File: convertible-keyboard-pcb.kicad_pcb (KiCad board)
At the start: 2 copper layers, 383 parts, among them J1 USB_C, Q1 AO3400A, Q2 2N7002, Q3 2N7002, SW1 SW_MX_LED, SW10 SW_MX_LED, SW100 SW_MX_LED, SW101 SW_MX_LED, SW102 SW_MX_LED, SW103 SW_MX_LED, SW104 SW_MX_LED, SW105 SW_MX_LED, SW106 SW_Push, SW107 SW_MX_LED, SW108 SW_MX_LED, SW11 SW_MX_LED, SW12 SW_MX_LED, SW13 SW_MX_LED, SW14 SW_MX_LED, SW15 SW_MX_LED, SW16 SW_MX_LED, SW17 SW_MX_LED, SW18 SW_MX_LED, SW19 SW_MX_LED, SW2 SW_MX_LED, SW20 SW_MX_LED, SW201 SW_Push, SW202 SW_Push, SW21 SW_MX_LED, SW22 SW_MX_LED, SW23 SW_MX_LED, SW24 SW_MX_LED, SW25 SW_MX_LED, SW26 SW_MX_LED, SW27 SW_MX_LED, SW28 SW_MX_LED, SW29 SW_MX_LED, SW3 SW_MX_LED, SW30 SW_MX_LED, SW31 SW_MX_LED, SW32 SW_MX_LED, SW33 SW_MX_LED, SW34 SW_MX_LED, SW35 SW_MX_LED, SW36 SW_MX_LED, SW37 SW_MX_LED, SW38 SW_MX_LED, SW39 SW_MX_LED, SW4 SW_MX_LED, SW40 SW_MX_LED, SW41 SW_MX_LED, SW42 SW_MX_LED, SW43 SW_MX_LED, SW44 SW_MX_LED, SW45 SW_MX_LED, SW46 SW_MX_LED, SW47 SW_MX_LED, SW48 SW_MX_LED, SW49 SW_MX_LED, SW5 SW_MX_LED, SW50 SW_MX_LED, SW51 SW_MX_LED, SW52 SW_MX_LED, SW53 SW_MX_LED, SW54 SW_MX_LED, SW55 SW_MX_LED, SW56 SW_MX_LED, SW57 SW_MX_LED, SW58 SW_MX_LED, SW59 SW_MX_LED, SW6 SW_MX_LED, SW60 SW_MX_LED, SW61 SW_MX_LED, SW62 SW_MX_LED, SW63 SW_MX_LED, SW64 SW_MX_LED, SW65 SW_MX_LED, SW66 SW_MX_LED, SW67 SW_MX_LED, SW68 SW_MX_LED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

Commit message: Lock-Anzeigen nur noch als 0805, TKL nur Caps Lock über BildAuf
- 3-mm-THT-Varianten entfernt (D121, D123, D125, D127)
- Über dem Numpad: D128 Num und D126 Caps mittig auf Höhe der F-Reihe,
  bestückt
- TKL: nur noch Caps Lock (D122, DNP) mittig über BildAuf in der Lücke
  zwischen F-Reihe und Zahlenreihe – Num Lock fällt mit dem Numpad ohnehin
  weg, daher Num-Anzeige D124 samt R128 entfernt
- Direkt in KiCad-Dateien geändert, nicht über tools/ – Generator-Stand
  endet mit 2eb5d4f (in tools/README und CLAUDE.md vermerkt)

ERC 0, Parität sauber, DRC ohne neue Meldungen.

Co-Authored-By: Claude Opus 5 (1M context) <noreply@anthropic.com>
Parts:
- removed D121, D123, D125, D127: 3mm, LED_THT:LED_D3.0mm
- removed D124: 0805, LED_SMD:LED_0805_2012Metric
- removed R128: 1k, Resistor_SMD:R_0603_1608Metric
- moved D122 10.4 mm to (366.7, 52.4)
- moved R127 8.82 mm to (370.7, 52.4)
- moved D126 3.40 mm to (428.6, 38.1)
- moved D128 3.40 mm to (409.6, 38.1)
- moved R130 2.26 mm to (413.6, 38.1)
- moved R129 2.24 mm to (432.6, 38.1)

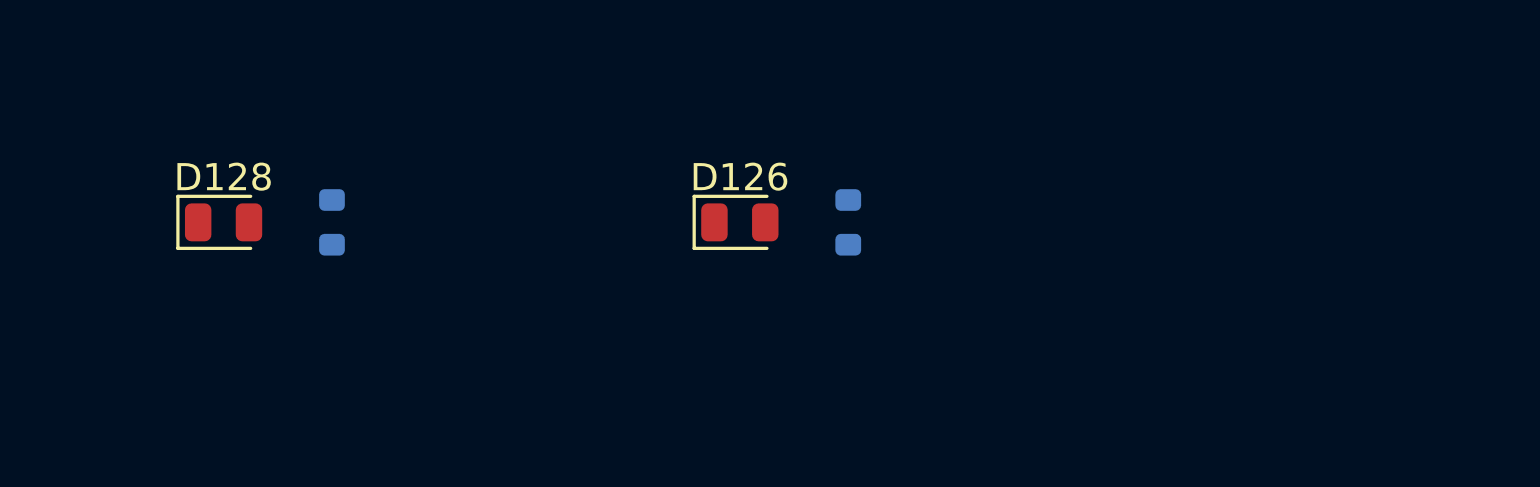
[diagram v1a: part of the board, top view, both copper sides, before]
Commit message: Lock-Anzeigen über dem Numpad rechtsbündig
Num Lock (D128) über *, Caps Lock (D126) über -, wie bei den meisten
Tastaturen; Vorwiderstände auf der Rückseite mitverschoben.

Co-Authored-By: Claude Opus 5 (1M context) <noreply@anthropic.com>
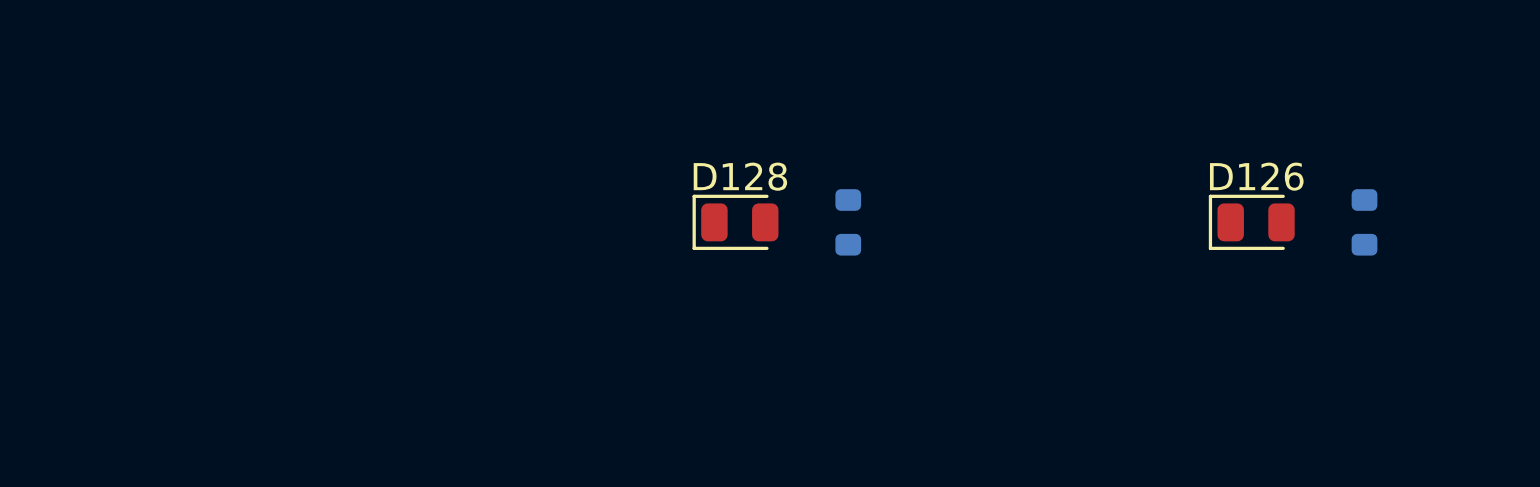
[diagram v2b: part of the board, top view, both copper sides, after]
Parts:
- moved D126 19.1 mm to (447.7, 38.1)
- moved D128 19.1 mm to (428.6, 38.1)
- moved R129 19.1 mm to (451.7, 38.1)
- moved R130 19.1 mm to (432.6, 38.1)
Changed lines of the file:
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@@
 	(footprint "LED_SMD:LED_0805_2012Metric"
 		(layer "F.Cu")
-		(at 409.575 38.1)
+		(at 428.625 38.1)
 		(descr "LED SMD 0805 (2012 Metric), square (rectangular) end terminal, IPC-7351 nominal, (Body size source: https://docs.google.com/spreadsheets/d/1BsfQQcO9C6DZCsRaXUlFlo91Tg2WpOkGARC1WS5S8t0/edit?usp=sharing)")
 		(tags "LED")
@@
 	(footprint "LED_SMD:LED_0805_2012Metric"
 		(layer "F.Cu")
-		(at 428.625 38.1)
+		(at 447.675 38.1)
 		(descr "LED SMD 0805 (2012 Metric), square (rectangular) end terminal, IPC-7351 nominal, (Body size source: https://docs.google.com/spreadsheets/d/1BsfQQcO9C6DZCsRaXUlFlo91Tg2WpOkGARC1WS5S8t0/edit?usp=sharing)")
 		(tags "LED")
@@
 	(footprint "Resistor_SMD:R_0603_1608Metric"
 		(layer "B.Cu")
-		(at 432.625 38.1 90)
+		(at 451.675 38.1 90)
 		(descr "Resistor SMD 0603 (1608 Metric), square (rectangular) end terminal, IPC-7351 nominal, (Body size source: IPC-SM-782 page 72, https://www.pcb-3d.com/wordpress/wp-content/uploads/ipc-sm-782a_amendment_1_and_2.pdf)")
 		(tags "resistor")
@@
 	(footprint "Resistor_SMD:R_0603_1608Metric"
 		(layer "B.Cu")
-		(at 413.575 38.1 90)
+		(at 432.625 38.1 90)
 		(descr "Resistor SMD 0603 (1608 Metric), square (rectangular) end terminal, IPC-7351 nominal, (Body size source: IPC-SM-782 page 72, https://www.pcb-3d.com/wordpress/wp-content/uploads/ipc-sm-782a_amendment_1_and_2.pdf)")
 		(tags "resistor")

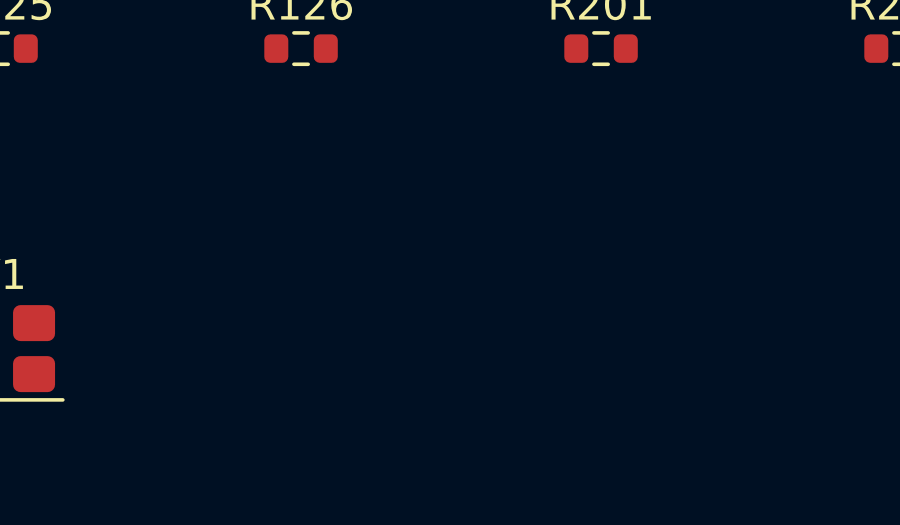
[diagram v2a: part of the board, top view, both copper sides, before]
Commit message: Anschlüsse für Unified Daughterboard (Pico-EZmate und JST-SH)
- J2 Molex Pico-EZmate 78171-0004 (uDB S1, C4, C5-EZM) und
  J3 JST-SH SM04B-SRSS-TB (uDB C3, C5-JSH), beide nicht bestückt
- Parallel zur USB-C-Buchse J1: Pin 1 VBUS, 2 D-, 3 D+, 4 + MP GND –
  Belegung aus den KiCad-Quellen von UDB-S und UDB-C-JSH gelesen (1:1-Kabel)
- J1 bleibt standardmäßig bestückt; für ein Daughterboard J1 weglassen und
  J2 oder J3 bestücken
- Footprints vorerst unplatziert neben den übrigen MCU-Bauteilen
- README (EN/DE) und CLAUDE.md ergänzt, LED-Entscheidung (THT oder
  Reverse-Mount-SMD) als offener Punkt vermerkt

ERC 0, Parität sauber, DRC ohne neue Meldungen.

Co-Authored-By: Claude Opus 5 (1M context) <noreply@anthropic.com>
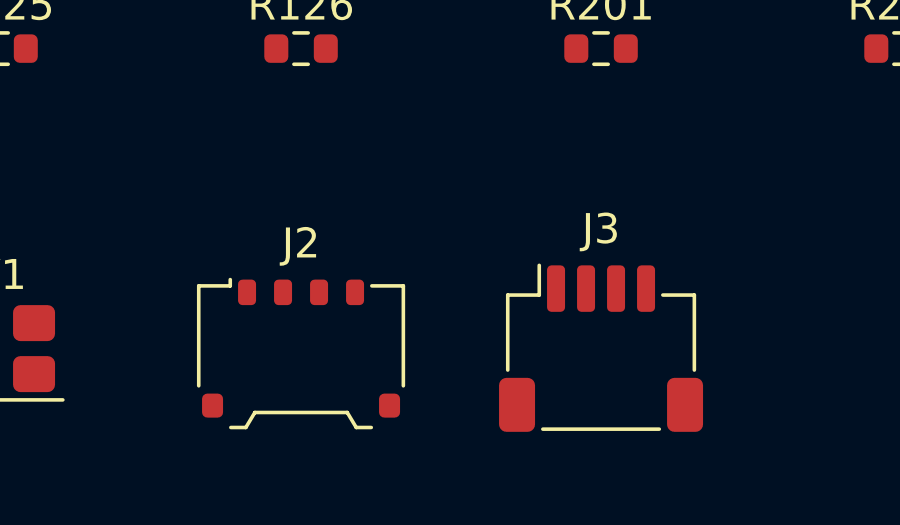
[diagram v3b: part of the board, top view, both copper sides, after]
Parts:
- added J2: Pico-EZmate 78171-0004, Connector_Molex:Molex_Pico-EZmate_78171-0004_1x04-1MP_P1.20mm_Vertical, F.Cu at (110.0, 195.0)
- added J3: JST-SH SM04B-SRSS-TB, Connector_JST:JST_SH_SM04B-SRSS-TB_1x04-1MP_P1.00mm_Horizontal, F.Cu at (120.0, 195.0)

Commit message: Tasten-LEDs als Reverse-Mount-SMD (Standard), THT-Variante vorgehalten
- Schalter wieder mit 2-Pin-Symbol und ai03-NoLED-Footprints; jede Taste
  hat eine eigene LED LEDn (gleiche Nummer) auf der Rückseite unter dem
  LED-Fenster (Schaltermitte +5,08 mm) – Drähte und Netze unverändert
- LED: XINGLIGHT XL-3216UWC-FB, weiß, LCSC C3646935, maschinell bestückt
- Eigener Footprint LED_1206_ReverseMount_XL-3216 nach dem JLC/EasyEDA-
  Footprint (Pads 1,0 x 1,524 mm bei +-1,651, Aussparung 2,2 x 1,9 mm):
  Pad-Innenkante 0,2 mm von der Aussparung, Eckradius 0,5 mm zum Fräsen.
  KiCads generischer Reverse-Mount-Footprint passt nicht zu diesem Teil
  (Loch in Längsrichtung kleiner als die Linse)
- convertible-keyboard-pcb.kicad_dru: 0,2 mm Kantenabstand nur an den
  LED-Aussparungen, sonst weiter 0,5 mm
- tools/led_variant.py smd|tht: tauscht nur die LED-Footprints; THT-Pads
  als MX_LED_THT/_FLIPPED in lib/keyboard.pretty, Hin- und Rückweg getestet
- Entfernt: Symbol SW_MX_LED, sym-lib-table, MXOnly-ISO-FLIPPED
  (FLIPPED-Sonderfälle entfallen mit den NoLED-Schaltern)
- README (EN/DE), tools/README, CLAUDE.md aktualisiert

ERC 0, Parität sauber, DRC ohne Fehler (nur bekannte Warnungen).

Co-Authored-By: Claude Opus 5 (1M context) <noreply@anthropic.com>
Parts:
- added LED1: XL-3216UWC-FB, keyboard:LED_1206_ReverseMount_XL-3216, B.Cu at (38.1, 43.2)
- added LED10: XL-3216UWC-FB, keyboard:LED_1206_ReverseMount_XL-3216, B.Cu at (247.7, 43.2)
- added LED100: XL-3216UWC-FB, keyboard:LED_1206_ReverseMount_XL-3216, B.Cu at (302.4, 148.0)
- added LED101: XL-3216UWC-FB, keyboard:LED_1206_ReverseMount_XL-3216, B.Cu at (328.6, 148.0)
- added LED102: XL-3216UWC-FB, keyboard:LED_1206_ReverseMount_XL-3216, B.Cu at (347.7, 148.0)
- added LED103: XL-3216UWC-FB, keyboard:LED_1206_ReverseMount_XL-3216, B.Cu at (366.7, 148.0)
- added LED104: XL-3216UWC-FB, keyboard:LED_1206_ReverseMount_XL-3216, B.Cu at (400.1, 148.0)
- added LED105: XL-3216UWC-FB, keyboard:LED_1206_ReverseMount_XL-3216, B.Cu at (428.6, 148.0)
- added LED107: XL-3216UWC-FB, keyboard:LED_1206_ReverseMount_XL-3216, B.Cu at (292.9, 109.9)
- added LED108: XL-3216UWC-FB, keyboard:LED_1206_ReverseMount_XL-3216, B.Cu at (50.0, 128.9)
- added LED11: XL-3216UWC-FB, keyboard:LED_1206_ReverseMount_XL-3216, B.Cu at (266.7, 43.2)
- added LED12: XL-3216UWC-FB, keyboard:LED_1206_ReverseMount_XL-3216, B.Cu at (285.8, 43.2)
- added LED13: XL-3216UWC-FB, keyboard:LED_1206_ReverseMount_XL-3216, B.Cu at (304.8, 43.2)
- added LED14: XL-3216UWC-FB, keyboard:LED_1206_ReverseMount_XL-3216, B.Cu at (328.6, 43.2)
- added LED15: XL-3216UWC-FB, keyboard:LED_1206_ReverseMount_XL-3216, B.Cu at (347.7, 43.2)
- added LED16: XL-3216UWC-FB, keyboard:LED_1206_ReverseMount_XL-3216, B.Cu at (366.7, 43.2)
- added LED17: XL-3216UWC-FB, keyboard:LED_1206_ReverseMount_XL-3216, B.Cu at (38.1, 71.8)
- added LED18: XL-3216UWC-FB, keyboard:LED_1206_ReverseMount_XL-3216, B.Cu at (57.1, 71.8)
- added LED19: XL-3216UWC-FB, keyboard:LED_1206_ReverseMount_XL-3216, B.Cu at (76.2, 71.8)
- added LED2: XL-3216UWC-FB, keyboard:LED_1206_ReverseMount_XL-3216, B.Cu at (76.2, 43.2)
- added LED20: XL-3216UWC-FB, keyboard:LED_1206_ReverseMount_XL-3216, B.Cu at (95.2, 71.8)
- added LED21: XL-3216UWC-FB, keyboard:LED_1206_ReverseMount_XL-3216, B.Cu at (114.3, 71.8)
- added LED22: XL-3216UWC-FB, keyboard:LED_1206_ReverseMount_XL-3216, B.Cu at (133.3, 71.8)
- added LED23: XL-3216UWC-FB, keyboard:LED_1206_ReverseMount_XL-3216, B.Cu at (152.4, 71.8)
- added LED24: XL-3216UWC-FB, keyboard:LED_1206_ReverseMount_XL-3216, B.Cu at (171.4, 71.8)
- added LED25: XL-3216UWC-FB, keyboard:LED_1206_ReverseMount_XL-3216, B.Cu at (190.5, 71.8)
- added LED26: XL-3216UWC-FB, keyboard:LED_1206_ReverseMount_XL-3216, B.Cu at (209.6, 71.8)
- added LED27: XL-3216UWC-FB, keyboard:LED_1206_ReverseMount_XL-3216, B.Cu at (228.6, 71.8)
- added LED28: XL-3216UWC-FB, keyboard:LED_1206_ReverseMount_XL-3216, B.Cu at (247.7, 71.8)
- added LED29: XL-3216UWC-FB, keyboard:LED_1206_ReverseMount_XL-3216, B.Cu at (266.7, 71.8)
- added LED3: XL-3216UWC-FB, keyboard:LED_1206_ReverseMount_XL-3216, B.Cu at (95.2, 43.2)
- added LED30: XL-3216UWC-FB, keyboard:LED_1206_ReverseMount_XL-3216, B.Cu at (295.3, 71.8)
- added LED31: XL-3216UWC-FB, keyboard:LED_1206_ReverseMount_XL-3216, B.Cu at (328.6, 71.8)
- added LED32: XL-3216UWC-FB, keyboard:LED_1206_ReverseMount_XL-3216, B.Cu at (347.7, 71.8)
- added LED33: XL-3216UWC-FB, keyboard:LED_1206_ReverseMount_XL-3216, B.Cu at (366.7, 71.8)
- added LED34: XL-3216UWC-FB, keyboard:LED_1206_ReverseMount_XL-3216, B.Cu at (390.5, 71.8)
- added LED35: XL-3216UWC-FB, keyboard:LED_1206_ReverseMount_XL-3216, B.Cu at (409.6, 71.8)
- added LED36: XL-3216UWC-FB, keyboard:LED_1206_ReverseMount_XL-3216, B.Cu at (428.6, 71.8)
- added LED37: XL-3216UWC-FB, keyboard:LED_1206_ReverseMount_XL-3216, B.Cu at (447.7, 71.8)
- added LED38: XL-3216UWC-FB, keyboard:LED_1206_ReverseMount_XL-3216, B.Cu at (42.9, 90.8)
- added LED39: XL-3216UWC-FB, keyboard:LED_1206_ReverseMount_XL-3216, B.Cu at (66.7, 90.8)
- added LED4: XL-3216UWC-FB, keyboard:LED_1206_ReverseMount_XL-3216, B.Cu at (114.3, 43.2)
- added LED40: XL-3216UWC-FB, keyboard:LED_1206_ReverseMount_XL-3216, B.Cu at (85.7, 90.8)
- added LED41: XL-3216UWC-FB, keyboard:LED_1206_ReverseMount_XL-3216, B.Cu at (104.8, 90.8)
- added LED42: XL-3216UWC-FB, keyboard:LED_1206_ReverseMount_XL-3216, B.Cu at (123.8, 90.8)
- added LED43: XL-3216UWC-FB, keyboard:LED_1206_ReverseMount_XL-3216, B.Cu at (142.9, 90.8)
- added LED44: XL-3216UWC-FB, keyboard:LED_1206_ReverseMount_XL-3216, B.Cu at (161.9, 90.8)
- added LED45: XL-3216UWC-FB, keyboard:LED_1206_ReverseMount_XL-3216, B.Cu at (181.0, 90.8)
- added LED46: XL-3216UWC-FB, keyboard:LED_1206_ReverseMount_XL-3216, B.Cu at (200.0, 90.8)
- added LED47: XL-3216UWC-FB, keyboard:LED_1206_ReverseMount_XL-3216, B.Cu at (219.1, 90.8)
- added LED48: XL-3216UWC-FB, keyboard:LED_1206_ReverseMount_XL-3216, B.Cu at (238.1, 90.8)
- added LED49: XL-3216UWC-FB, keyboard:LED_1206_ReverseMount_XL-3216, B.Cu at (257.2, 90.8)
- added LED5: XL-3216UWC-FB, keyboard:LED_1206_ReverseMount_XL-3216, B.Cu at (133.3, 43.2)
- added LED50: XL-3216UWC-FB, keyboard:LED_1206_ReverseMount_XL-3216, B.Cu at (276.2, 90.8)
- added LED51: XL-3216UWC-FB, keyboard:LED_1206_ReverseMount_XL-3216, B.Cu at (328.6, 90.8)
- added LED52: XL-3216UWC-FB, keyboard:LED_1206_ReverseMount_XL-3216, B.Cu at (347.7, 90.8)
- added LED53: XL-3216UWC-FB, keyboard:LED_1206_ReverseMount_XL-3216, B.Cu at (366.7, 90.8)
- added LED54: XL-3216UWC-FB, keyboard:LED_1206_ReverseMount_XL-3216, B.Cu at (390.5, 90.8)
- added LED55: XL-3216UWC-FB, keyboard:LED_1206_ReverseMount_XL-3216, B.Cu at (409.6, 90.8)
- added LED56: XL-3216UWC-FB, keyboard:LED_1206_ReverseMount_XL-3216, B.Cu at (428.6, 90.8)
- added LED57: XL-3216UWC-FB, keyboard:LED_1206_ReverseMount_XL-3216, B.Cu at (447.7, 100.3)
- added LED58: XL-3216UWC-FB, keyboard:LED_1206_ReverseMount_XL-3216, B.Cu at (45.2, 109.9)
- added LED59: XL-3216UWC-FB, keyboard:LED_1206_ReverseMount_XL-3216, B.Cu at (71.4, 109.9)
- added LED6: XL-3216UWC-FB, keyboard:LED_1206_ReverseMount_XL-3216, B.Cu at (161.9, 43.2)
- added LED60: XL-3216UWC-FB, keyboard:LED_1206_ReverseMount_XL-3216, B.Cu at (90.5, 109.9)
- added LED61: XL-3216UWC-FB, keyboard:LED_1206_ReverseMount_XL-3216, B.Cu at (109.5, 109.9)
- added LED62: XL-3216UWC-FB, keyboard:LED_1206_ReverseMount_XL-3216, B.Cu at (128.6, 109.9)
- added LED63: XL-3216UWC-FB, keyboard:LED_1206_ReverseMount_XL-3216, B.Cu at (147.6, 109.9)
- added LED64: XL-3216UWC-FB, keyboard:LED_1206_ReverseMount_XL-3216, B.Cu at (166.7, 109.9)
- added LED65: XL-3216UWC-FB, keyboard:LED_1206_ReverseMount_XL-3216, B.Cu at (185.7, 109.9)
- added LED66: XL-3216UWC-FB, keyboard:LED_1206_ReverseMount_XL-3216, B.Cu at (204.8, 109.9)
- added LED67: XL-3216UWC-FB, keyboard:LED_1206_ReverseMount_XL-3216, B.Cu at (223.8, 109.9)
- added LED68: XL-3216UWC-FB, keyboard:LED_1206_ReverseMount_XL-3216, B.Cu at (242.9, 109.9)
- added LED69: XL-3216UWC-FB, keyboard:LED_1206_ReverseMount_XL-3216, B.Cu at (261.9, 109.9)
- added LED7: XL-3216UWC-FB, keyboard:LED_1206_ReverseMount_XL-3216, B.Cu at (181.0, 43.2)
- added LED70: XL-3216UWC-FB, keyboard:LED_1206_ReverseMount_XL-3216, B.Cu at (281.0, 109.9)
- added LED71: XL-3216UWC-FB, keyboard:LED_1206_ReverseMount_XL-3216, B.Cu at (302.4, 100.3)
- added LED72: XL-3216UWC-FB, keyboard:LED_1206_ReverseMount_XL-3216, B.Cu at (390.5, 109.9)
- added LED73: XL-3216UWC-FB, keyboard:LED_1206_ReverseMount_XL-3216, B.Cu at (409.6, 109.9)
- added LED74: XL-3216UWC-FB, keyboard:LED_1206_ReverseMount_XL-3216, B.Cu at (428.6, 109.9)
- added LED75: XL-3216UWC-FB, keyboard:LED_1206_ReverseMount_XL-3216, B.Cu at (40.5, 128.9)
- added LED76: XL-3216UWC-FB, keyboard:LED_1206_ReverseMount_XL-3216, B.Cu at (61.9, 128.9)
- added LED77: XL-3216UWC-FB, keyboard:LED_1206_ReverseMount_XL-3216, B.Cu at (81.0, 128.9)
- added LED78: XL-3216UWC-FB, keyboard:LED_1206_ReverseMount_XL-3216, B.Cu at (100.0, 128.9)
- added LED79: XL-3216UWC-FB, keyboard:LED_1206_ReverseMount_XL-3216, B.Cu at (119.1, 128.9)
- added LED8: XL-3216UWC-FB, keyboard:LED_1206_ReverseMount_XL-3216, B.Cu at (200.0, 43.2)
- added LED80: XL-3216UWC-FB, keyboard:LED_1206_ReverseMount_XL-3216, B.Cu at (138.1, 128.9)
- added LED81: XL-3216UWC-FB, keyboard:LED_1206_ReverseMount_XL-3216, B.Cu at (157.2, 128.9)
- added LED82: XL-3216UWC-FB, keyboard:LED_1206_ReverseMount_XL-3216, B.Cu at (176.2, 128.9)
- added LED83: XL-3216UWC-FB, keyboard:LED_1206_ReverseMount_XL-3216, B.Cu at (195.3, 128.9)
- added LED84: XL-3216UWC-FB, keyboard:LED_1206_ReverseMount_XL-3216, B.Cu at (214.3, 128.9)
- added LED85: XL-3216UWC-FB, keyboard:LED_1206_ReverseMount_XL-3216, B.Cu at (233.4, 128.9)
- added LED86: XL-3216UWC-FB, keyboard:LED_1206_ReverseMount_XL-3216, B.Cu at (252.4, 128.9)
- added LED87: XL-3216UWC-FB, keyboard:LED_1206_ReverseMount_XL-3216, B.Cu at (288.1, 128.9)
- added LED88: XL-3216UWC-FB, keyboard:LED_1206_ReverseMount_XL-3216, B.Cu at (347.7, 128.9)
- added LED89: XL-3216UWC-FB, keyboard:LED_1206_ReverseMount_XL-3216, B.Cu at (390.5, 128.9)
- added LED9: XL-3216UWC-FB, keyboard:LED_1206_ReverseMount_XL-3216, B.Cu at (219.1, 43.2)
- added LED90: XL-3216UWC-FB, keyboard:LED_1206_ReverseMount_XL-3216, B.Cu at (409.6, 128.9)
- added LED91: XL-3216UWC-FB, keyboard:LED_1206_ReverseMount_XL-3216, B.Cu at (428.6, 128.9)
- added LED92: XL-3216UWC-FB, keyboard:LED_1206_ReverseMount_XL-3216, B.Cu at (447.7, 138.4)
- added LED93: XL-3216UWC-FB, keyboard:LED_1206_ReverseMount_XL-3216, B.Cu at (40.5, 148.0)
- added LED94: XL-3216UWC-FB, keyboard:LED_1206_ReverseMount_XL-3216, B.Cu at (64.3, 148.0)
- added LED95: XL-3216UWC-FB, keyboard:LED_1206_ReverseMount_XL-3216, B.Cu at (88.1, 148.0)
- added LED96: XL-3216UWC-FB, keyboard:LED_1206_ReverseMount_XL-3216, B.Cu at (159.5, 148.0)
- added LED97: XL-3216UWC-FB, keyboard:LED_1206_ReverseMount_XL-3216, B.Cu at (231.0, 148.0)
- added LED98: XL-3216UWC-FB, keyboard:LED_1206_ReverseMount_XL-3216, B.Cu at (254.8, 148.0)
- added LED99: XL-3216UWC-FB, keyboard:LED_1206_ReverseMount_XL-3216, B.Cu at (278.6, 148.0)
- SW1, SW10, SW101, SW102, SW103, SW105, SW11, SW12, SW13, SW14, SW15, SW16, SW17, SW18, SW19, SW2, SW20, SW21, SW22, SW23, SW24, SW25, SW26, SW27, SW28, SW29, SW3, SW31, SW32, SW33, SW34, SW35, SW36, SW37, SW39, SW4, SW40, SW41, SW42, SW43, SW44, SW45, SW46, SW47, SW48, SW49, SW5, SW50, SW51, SW52, SW53, SW54, SW55, SW56, SW59, SW6, SW60, SW61, SW62, SW63, SW64, SW65, SW66, SW67, SW68, SW69, SW7, SW70, SW72, SW73, SW74, SW77, SW78, SW79, SW8, SW80, SW81, SW82, SW83, SW84, SW85, SW86, SW88, SW89, SW9, SW90, SW91: value SW_MX_LED -> SW_Push; footprint MX_Only:MXOnly-1U -> MX_Only:MXOnly-1U-NoLED
- SW100, SW75, SW93, SW94, SW95, SW97, SW98, SW99: value SW_MX_LED -> SW_Push; footprint MX_Only:MXOnly-1.25U -> MX_Only:MXOnly-1.25U-NoLED
- SW104, SW30: value SW_MX_LED -> SW_Push; footprint MX_Only:MXOnly-2U -> MX_Only:MXOnly-2U-NoLED
- SW107: value SW_MX_LED -> SW_Push; footprint MX_Only:MXOnly-2.25U-FLIPPED -> MX_Only:MXOnly-2.25U-NoLED
- SW108: value SW_MX_LED -> SW_Push; footprint MX_Only:MXOnly-2.25U -> MX_Only:MXOnly-2.25U-NoLED
- SW38: value SW_MX_LED -> SW_Push; footprint MX_Only:MXOnly-1.5U -> MX_Only:MXOnly-1.5U-NoLED
- SW57, SW92: value SW_MX_LED -> SW_Push; footprint MX_Only:MXOnly-2U-VerticalStabilizers -> MX_Only:MXOnly-2U-VerticalStabilizers-NoLED
- SW58: value SW_MX_LED -> SW_Push; footprint MX_Only:MXOnly-1.75U -> MX_Only:MXOnly-1.75U-NoLED
- SW71: value SW_MX_LED -> SW_Push; footprint keyboard:MXOnly-ISO-FLIPPED -> MX_Only:MXOnly-ISO-NoLED
- SW76: value SW_MX_LED -> SW_Push; footprint MX_Only:MXOnly-1U-FLIPPED -> MX_Only:MXOnly-1U-NoLED
- SW87: value SW_MX_LED -> SW_Push; footprint MX_Only:MXOnly-2.75U -> MX_Only:MXOnly-2.75U-NoLED
- SW96: value SW_MX_LED -> SW_Push; footprint MX_Only:MXOnly-6.25U -> MX_Only:MXOnly-6.25U-NoLED
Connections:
- R1 pad 2: Net-(SW1B-A) -> Net-(LED1-A)
- R10 pad 2: Net-(SW10B-A) -> Net-(LED10-A)
- R100 pad 2: Net-(SW100B-A) -> Net-(LED100-A)
- R101 pad 2: Net-(SW101B-A) -> Net-(LED101-A)
- R102 pad 2: Net-(SW102B-A) -> Net-(LED102-A)
- R103 pad 2: Net-(SW103B-A) -> Net-(LED103-A)
- R104 pad 2: Net-(SW104B-A) -> Net-(LED104-A)
- R105 pad 2: Net-(SW105B-A) -> Net-(LED105-A)
- R107 pad 2: Net-(SW107B-A) -> Net-(LED107-A)
- R108 pad 2: Net-(SW108B-A) -> Net-(LED108-A)
- R11 pad 2: Net-(SW11B-A) -> Net-(LED11-A)
- R12 pad 2: Net-(SW12B-A) -> Net-(LED12-A)
- R13 pad 2: Net-(SW13B-A) -> Net-(LED13-A)
- R14 pad 2: Net-(SW14B-A) -> Net-(LED14-A)
- R15 pad 2: Net-(SW15B-A) -> Net-(LED15-A)
- R16 pad 2: Net-(SW16B-A) -> Net-(LED16-A)
- R17 pad 2: Net-(SW17B-A) -> Net-(LED17-A)
- R18 pad 2: Net-(SW18B-A) -> Net-(LED18-A)
- R19 pad 2: Net-(SW19B-A) -> Net-(LED19-A)
- R2 pad 2: Net-(SW2B-A) -> Net-(LED2-A)
- R20 pad 2: Net-(SW20B-A) -> Net-(LED20-A)
- R21 pad 2: Net-(SW21B-A) -> Net-(LED21-A)
- R22 pad 2: Net-(SW22B-A) -> Net-(LED22-A)
- R23 pad 2: Net-(SW23B-A) -> Net-(LED23-A)
- R24 pad 2: Net-(SW24B-A) -> Net-(LED24-A)
- R25 pad 2: Net-(SW25B-A) -> Net-(LED25-A)
- R26 pad 2: Net-(SW26B-A) -> Net-(LED26-A)
- R27 pad 2: Net-(SW27B-A) -> Net-(LED27-A)
- R28 pad 2: Net-(SW28B-A) -> Net-(LED28-A)
- R29 pad 2: Net-(SW29B-A) -> Net-(LED29-A)
- R3 pad 2: Net-(SW3B-A) -> Net-(LED3-A)
- R30 pad 2: Net-(SW30B-A) -> Net-(LED30-A)
- R31 pad 2: Net-(SW31B-A) -> Net-(LED31-A)
- R32 pad 2: Net-(SW32B-A) -> Net-(LED32-A)
- R33 pad 2: Net-(SW33B-A) -> Net-(LED33-A)
- R34 pad 2: Net-(SW34B-A) -> Net-(LED34-A)
- R35 pad 2: Net-(SW35B-A) -> Net-(LED35-A)
- R36 pad 2: Net-(SW36B-A) -> Net-(LED36-A)
- R37 pad 2: Net-(SW37B-A) -> Net-(LED37-A)
- R38 pad 2: Net-(SW38B-A) -> Net-(LED38-A)
- R39 pad 2: Net-(SW39B-A) -> Net-(LED39-A)
- R4 pad 2: Net-(SW4B-A) -> Net-(LED4-A)
- R40 pad 2: Net-(SW40B-A) -> Net-(LED40-A)
- R41 pad 2: Net-(SW41B-A) -> Net-(LED41-A)
- R42 pad 2: Net-(SW42B-A) -> Net-(LED42-A)
- R43 pad 2: Net-(SW43B-A) -> Net-(LED43-A)
- R44 pad 2: Net-(SW44B-A) -> Net-(LED44-A)
- R45 pad 2: Net-(SW45B-A) -> Net-(LED45-A)
- R46 pad 2: Net-(SW46B-A) -> Net-(LED46-A)
- R47 pad 2: Net-(SW47B-A) -> Net-(LED47-A)
- R48 pad 2: Net-(SW48B-A) -> Net-(LED48-A)
- R49 pad 2: Net-(SW49B-A) -> Net-(LED49-A)
- R5 pad 2: Net-(SW5B-A) -> Net-(LED5-A)
- R50 pad 2: Net-(SW50B-A) -> Net-(LED50-A)
- R51 pad 2: Net-(SW51B-A) -> Net-(LED51-A)
- R52 pad 2: Net-(SW52B-A) -> Net-(LED52-A)
- R53 pad 2: Net-(SW53B-A) -> Net-(LED53-A)
- R54 pad 2: Net-(SW54B-A) -> Net-(LED54-A)
- R55 pad 2: Net-(SW55B-A) -> Net-(LED55-A)
- R56 pad 2: Net-(SW56B-A) -> Net-(LED56-A)
- R57 pad 2: Net-(SW57B-A) -> Net-(LED57-A)
- R58 pad 2: Net-(SW58B-A) -> Net-(LED58-A)
- R59 pad 2: Net-(SW59B-A) -> Net-(LED59-A)
- R6 pad 2: Net-(SW6B-A) -> Net-(LED6-A)
- R60 pad 2: Net-(SW60B-A) -> Net-(LED60-A)
- R61 pad 2: Net-(SW61B-A) -> Net-(LED61-A)
- R62 pad 2: Net-(SW62B-A) -> Net-(LED62-A)
- R63 pad 2: Net-(SW63B-A) -> Net-(LED63-A)
- R64 pad 2: Net-(SW64B-A) -> Net-(LED64-A)
- R65 pad 2: Net-(SW65B-A) -> Net-(LED65-A)
- R66 pad 2: Net-(SW66B-A) -> Net-(LED66-A)
- R67 pad 2: Net-(SW67B-A) -> Net-(LED67-A)
- R68 pad 2: Net-(SW68B-A) -> Net-(LED68-A)
- R69 pad 2: Net-(SW69B-A) -> Net-(LED69-A)
- R7 pad 2: Net-(SW7B-A) -> Net-(LED7-A)
- R70 pad 2: Net-(SW70B-A) -> Net-(LED70-A)
- R71 pad 2: Net-(SW71B-A) -> Net-(LED71-A)
- R72 pad 2: Net-(SW72B-A) -> Net-(LED72-A)
- R73 pad 2: Net-(SW73B-A) -> Net-(LED73-A)
- R74 pad 2: Net-(SW74B-A) -> Net-(LED74-A)
- R75 pad 2: Net-(SW75B-A) -> Net-(LED75-A)
- R76 pad 2: Net-(SW76B-A) -> Net-(LED76-A)
- R77 pad 2: Net-(SW77B-A) -> Net-(LED77-A)
- R78 pad 2: Net-(SW78B-A) -> Net-(LED78-A)
- R79 pad 2: Net-(SW79B-A) -> Net-(LED79-A)
- R8 pad 2: Net-(SW8B-A) -> Net-(LED8-A)
- R80 pad 2: Net-(SW80B-A) -> Net-(LED80-A)
- R81 pad 2: Net-(SW81B-A) -> Net-(LED81-A)
- R82 pad 2: Net-(SW82B-A) -> Net-(LED82-A)
- R83 pad 2: Net-(SW83B-A) -> Net-(LED83-A)
- R84 pad 2: Net-(SW84B-A) -> Net-(LED84-A)
- R85 pad 2: Net-(SW85B-A) -> Net-(LED85-A)
- R86 pad 2: Net-(SW86B-A) -> Net-(LED86-A)
- R87 pad 2: Net-(SW87B-A) -> Net-(LED87-A)
- R88 pad 2: Net-(SW88B-A) -> Net-(LED88-A)
- R89 pad 2: Net-(SW89B-A) -> Net-(LED89-A)
- R9 pad 2: Net-(SW9B-A) -> Net-(LED9-A)
- R90 pad 2: Net-(SW90B-A) -> Net-(LED90-A)
- R91 pad 2: Net-(SW91B-A) -> Net-(LED91-A)
- R92 pad 2: Net-(SW92B-A) -> Net-(LED92-A)
- R93 pad 2: Net-(SW93B-A) -> Net-(LED93-A)
- R94 pad 2: Net-(SW94B-A) -> Net-(LED94-A)
- R95 pad 2: Net-(SW95B-A) -> Net-(LED95-A)
- R96 pad 2: Net-(SW96B-A) -> Net-(LED96-A)
- R97 pad 2: Net-(SW97B-A) -> Net-(LED97-A)
- R98 pad 2: Net-(SW98B-A) -> Net-(LED98-A)
- R99 pad 2: Net-(SW99B-A) -> Net-(LED99-A)
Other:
- board outline added: 2.2 x 1.9 mm
